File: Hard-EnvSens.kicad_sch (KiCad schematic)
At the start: 60 parts, among them P1 USB_C_Plug_USB2.0, P2 USB_C_Plug_USB2.0, Q1 SS8050, Q2 SS8050, SW1 SW_Push, SW3 SW_Push, U1 LD1117S33TR_SOT223, U2 ESP32-C6-WROOM-1, U3 CP2104, U4 VEML7700-TR, U5 DPS368, U6 SGP41-D-R4, U7 SHT40-AD1B-R2, U8 AS7341-DLGT, U9 TPS79318DBVTG4

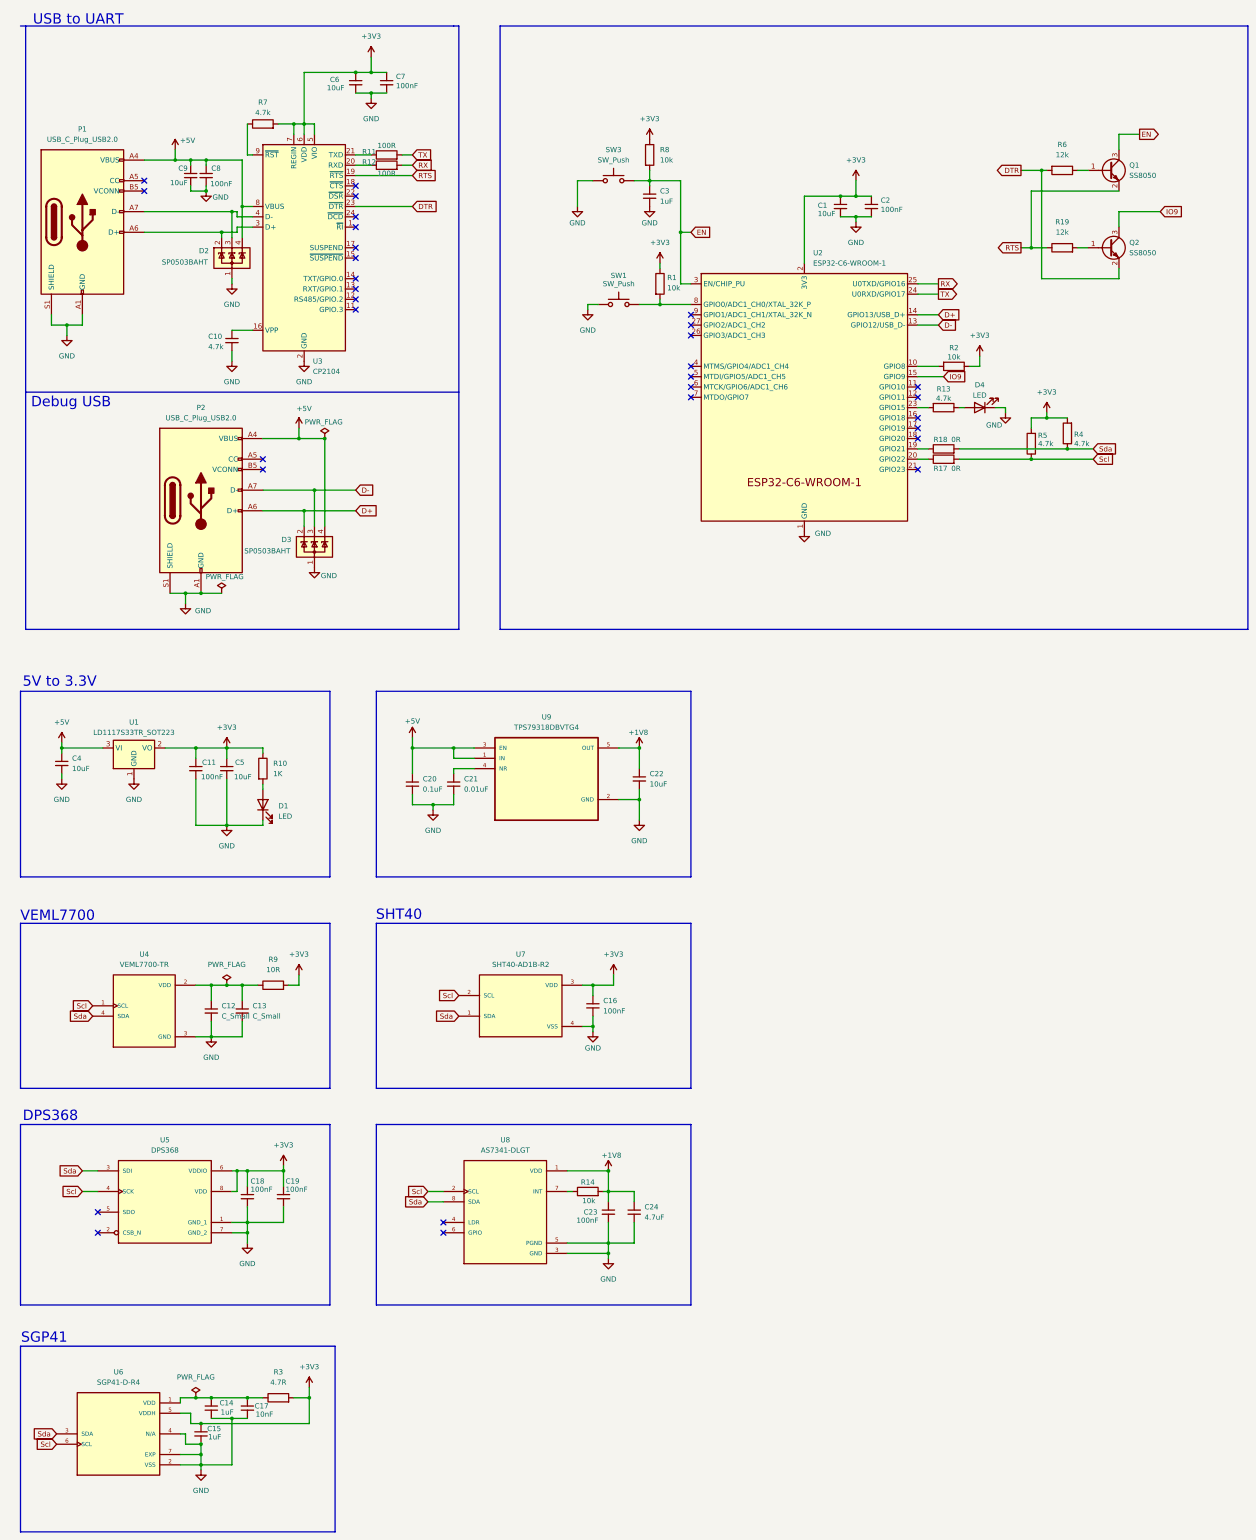
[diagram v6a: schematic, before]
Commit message: Schematic done, Bottom board
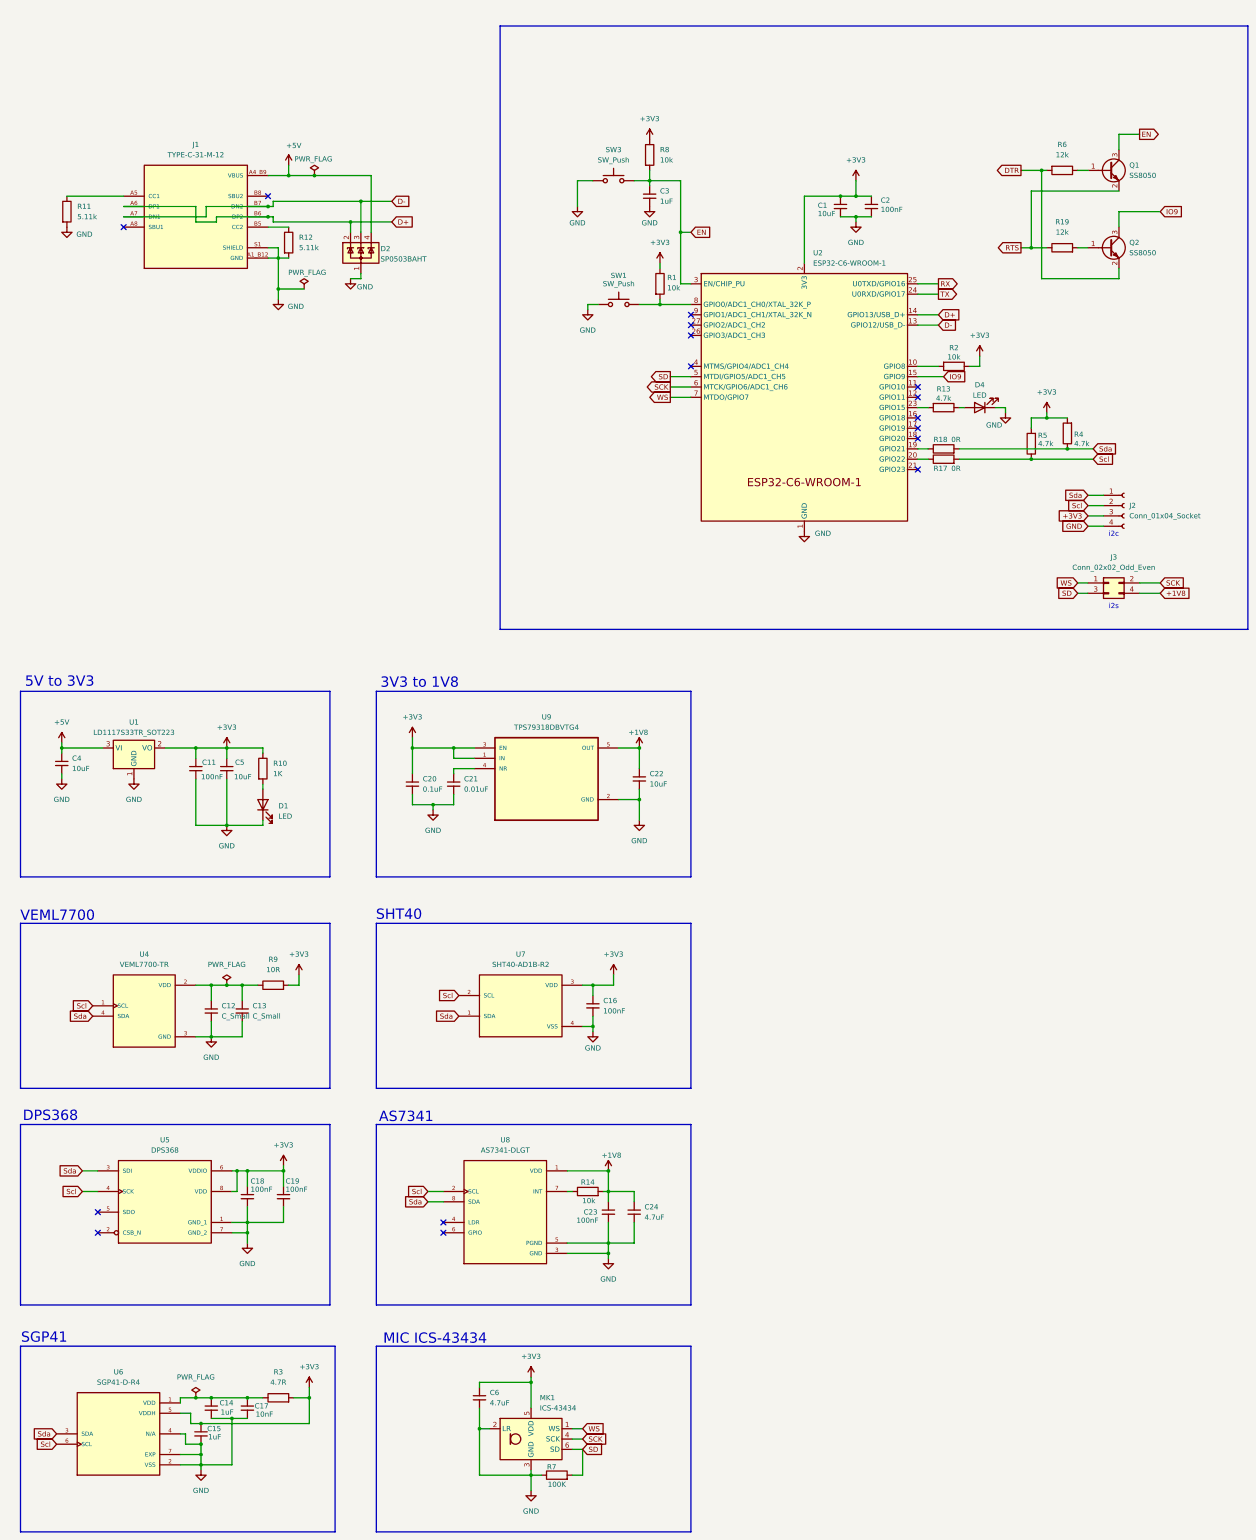
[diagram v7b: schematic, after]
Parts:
- removed C10: 4.7k, symbol Device:C_Small
- removed C7, C8: 100nF, symbol Device:C_Small
- removed C9: 10uF, symbol Device:C_Small
- removed D3: SP0503BAHT, Package_TO_SOT_SMD:SOT-143, symbol Power_Protection:SP0503BAHT
- removed P1, P2: USB_C_Plug_USB2.0, symbol Connector:USB_C_Plug_USB2.0
- removed U3: CP2104, Package_DFN_QFN:QFN-24-1EP_4x4mm_P0.5mm_EP2.6x2.6mm, symbol Interface_USB:CP2104
- added J1: TYPE-C-31-M-12, Biblioteca_Kicad:HRO_TYPE-C-31-M-12, symbol TYPE-C-31-M-12:TYPE-C-31-M-12
- added J2: Conn_01x04_Socket, Connector_PinSocket_2.54mm:PinSocket_1x04_P2.54mm_Vertical, symbol Connector:Conn_01x04_Socket
- added J3: Conn_02x02_Odd_Even, Connector_PinSocket_2.54mm:PinSocket_2x02_P2.54mm_Vertical, symbol Connector_Generic:Conn_02x02_Odd_Even
- added MK1: ICS-43434, Sensor_Audio:InvenSense_ICS-43434-6_3.5x2.65mm, symbol Sensor_Audio:ICS-43434
- C1, C11, C12, C13, C14, C15, C16, C17, C18, C19, C2, C20, C21, C22, C23, C24, C3, C4, C5: footprint (none) -> Capacitor_SMD:C_0603_1608Metric
- C6: value 10uF -> 4.7uF; footprint (none) -> Capacitor_SMD:C_0603_1608Metric
- D1, D4: footprint (none) -> LED_SMD:LED_0603_1608Metric
- R1, R10, R13, R14, R17, R18, R19, R2, R3, R4, R5, R6, R8, R9: footprint (none) -> Resistor_SMD:R_0603_1608Metric
- R11, R12: value 100R -> 5.11k; footprint (none) -> Resistor_SMD:R_0603_1608Metric
- R7: value 4.7k -> 100K; footprint (none) -> Resistor_SMD:R_0603_1608Metric
- SW1, SW3: footprint (none) -> Biblioteca_Kicad:SW_3-1437565-0
- U8: footprint AS7341-DLGT:PSON80P310X200X110-8N -> Package_LGA:AMS_OLGA-8_2x3.1mm_P0.8mm
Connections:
- net +1V8: now also J3.4 (Pin_4)
- net +3V3: now also C20.1, U9.1 (IN), U9.3 (EN), J2.3 (Pin_3), MK1.5 (VDD); no longer R7.2
- net +5V: now also J1.A4_B9 (VBUS), J1.B4_A9 (VBUS); no longer C20.1, U9.1 (IN), U9.3 (EN)
- net D+: now also D2.2 (K), J1.A6 (DP1), J1.B6 (DP2)
- net D-: now also D2.3 (K), J1.A7 (DN1), J1.B7 (DN2)
- net GND: now also R11.2, R12.2, R7.1, J1.A1_B12 (GND), J1.B1_A12 (GND), J1.S1 (SHIELD), J1.S2 (SHIELD), J1.S3 (SHIELD), J1.S4 (SHIELD), J2.4 (Pin_4), MK1.2 (LR), MK1.3 (GND)
- net RX: no longer R12.2
- net Scl: now also J2.2 (Pin_2)
- net Sda: now also J2.1 (Pin_1)
- net TX: no longer R11.2
- net at R12.1: now also J1.B5 (CC2)
- net at R11.1: now also J1.A5 (CC1)
- net SD: now reaches U2.5 (MTDI/GPIO5/ADC1_CH5)
- net SD: now also R7.2, J3.3 (Pin_3), MK1.6 (SD)
- net SCK: now reaches U2.6 (MTCK/GPIO6/ADC1_CH6)
- net SCK: now also J3.2 (Pin_2), MK1.4 (SCK)
- net WS: now reaches U2.7 (MTDO/GPIO7)
- net WS: now also J3.1 (Pin_1), MK1.1 (WS)
- no-connect marks 31 -> 16
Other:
- note added: "3V3 to 1V8"
- note added: "5V to 3V3"
- note added: "AS7341"
- note added: "MIC ICS-43434"
- note added: "i2c"
- note added: "i2s"
- note removed: "5V to 3.3V"
- note removed: "Debug USB"
- note removed: "USB to UART"

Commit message: Started connections and sensors pcb
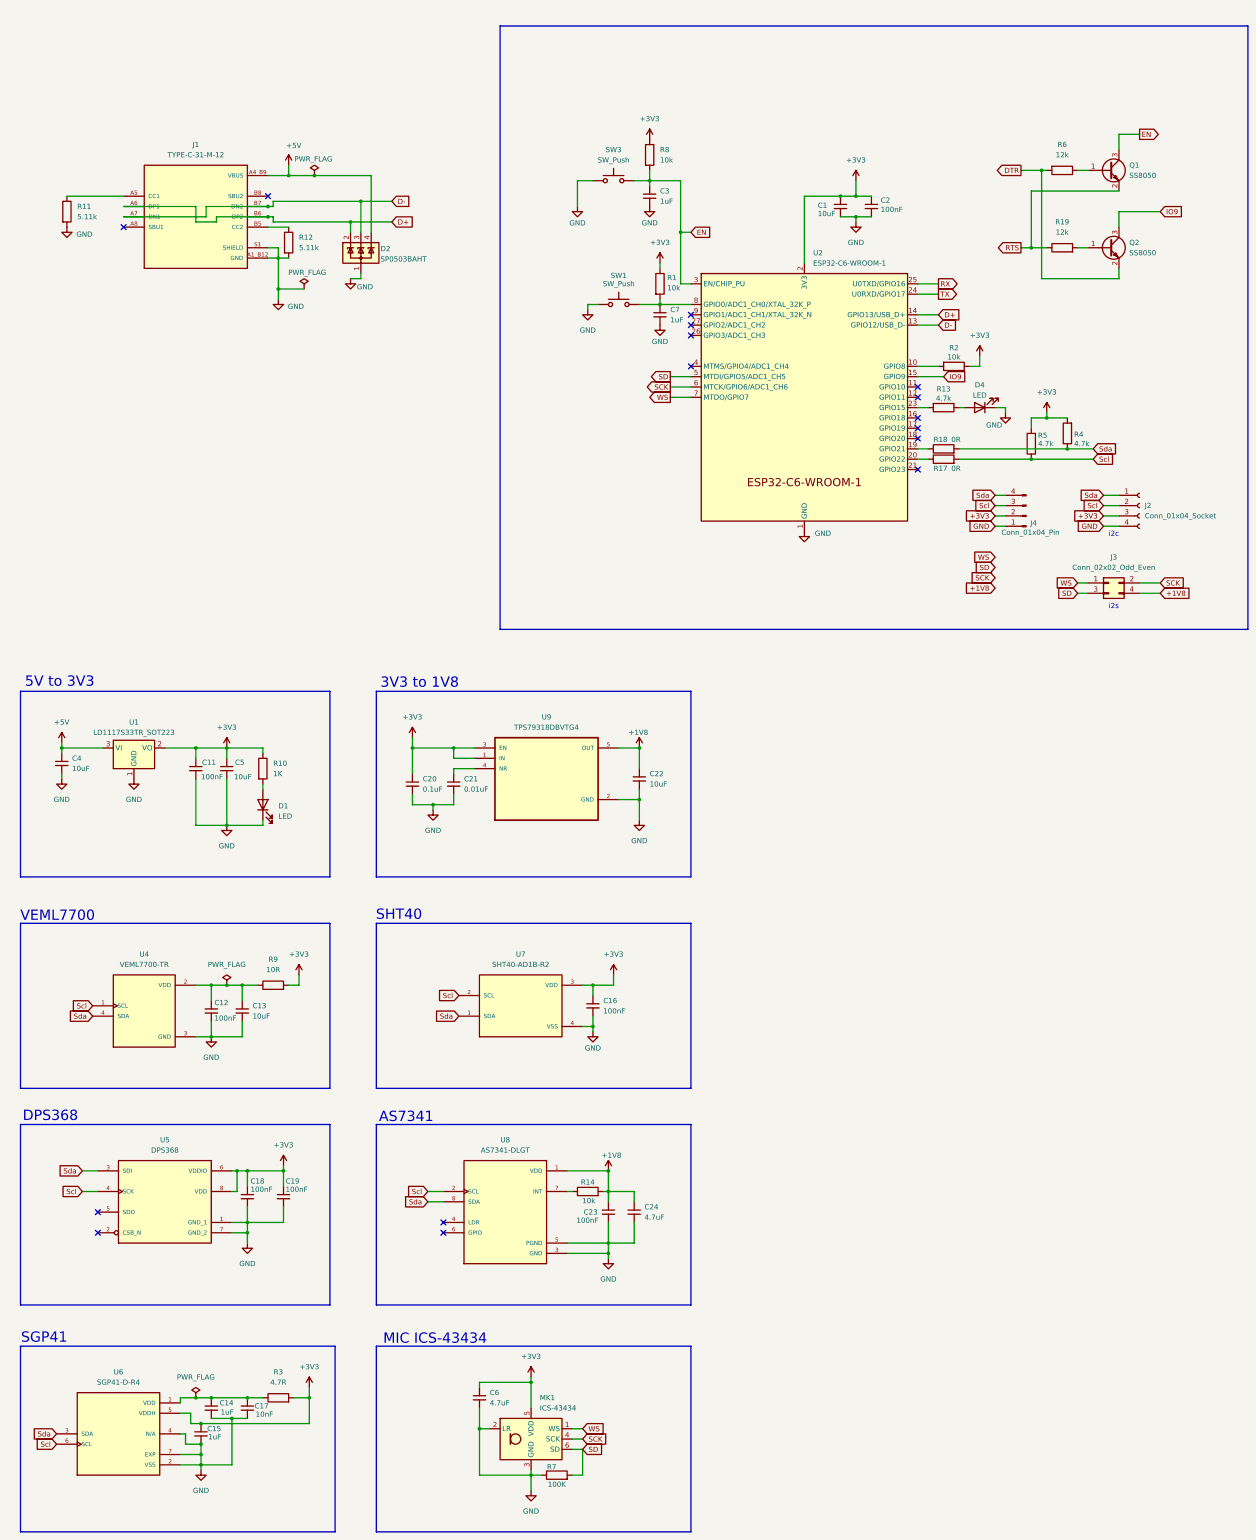
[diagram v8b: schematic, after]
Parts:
- added C7: 1uF, Capacitor_SMD:C_0603_1608Metric, symbol Device:C_Small
- added J4: Conn_01x04_Pin, symbol Connector:Conn_01x04_Pin
- C12: value C_Small -> 100nF
- C13: value C_Small -> 10uF
- U9: footprint TPS79318DBVTG4:SOT95P280X145-5N -> libs:SOT95P280X145-5N
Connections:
- net +3V3: now also J4.2 (Pin_2)
- net GND: now also C7.2, J4.1 (Pin_1)
- net Scl: now also J4.3 (Pin_3)
- net Sda: now also J4.4 (Pin_4)
- net at R1.2, SW1.2, U2.8 (GPIO0/ADC1_CH0/XTAL_32K_P): now also C7.1
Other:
- moved on the sheet: J2
